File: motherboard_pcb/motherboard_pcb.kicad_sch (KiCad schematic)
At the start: 10 parts, among them J1 24 Power Supply Input, J2 Conn_01x04_Socket, J3 Conn_01x04_Socket, J4 Conn_01x04_Socket, J5 Conn_01x04_Socket, U1 ESP32-DEVKIT-V1

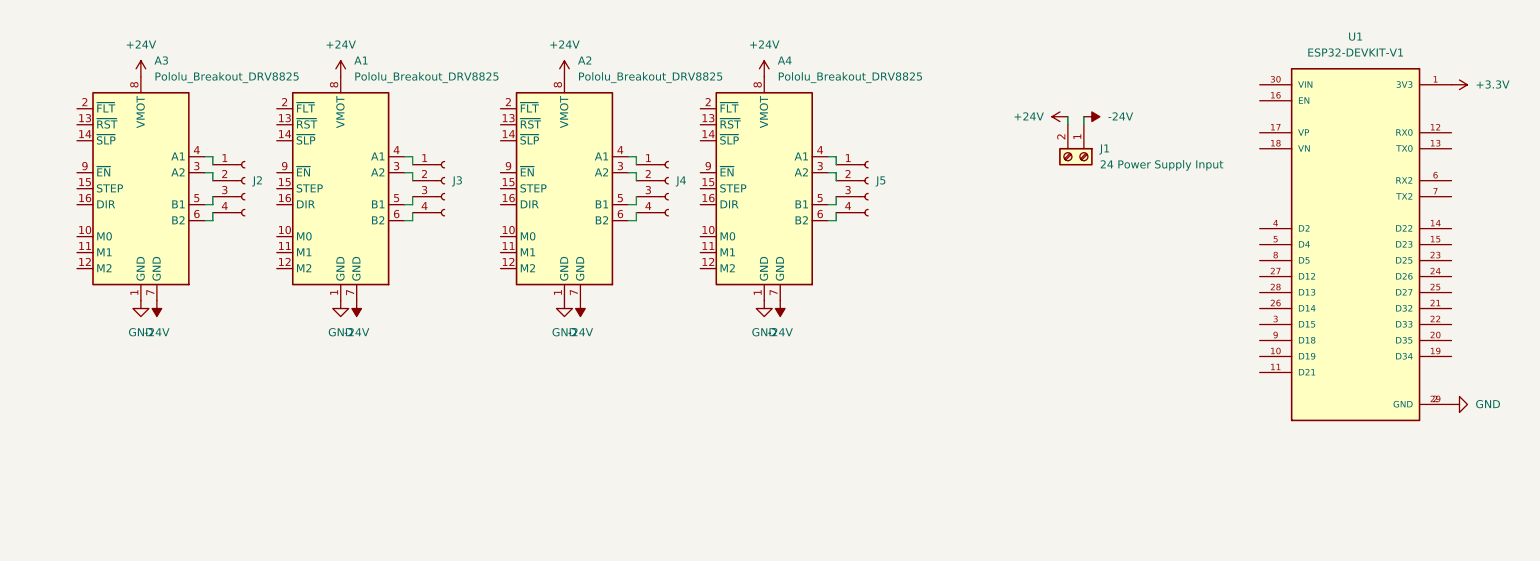
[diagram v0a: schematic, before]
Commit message: Added connections for OLED display
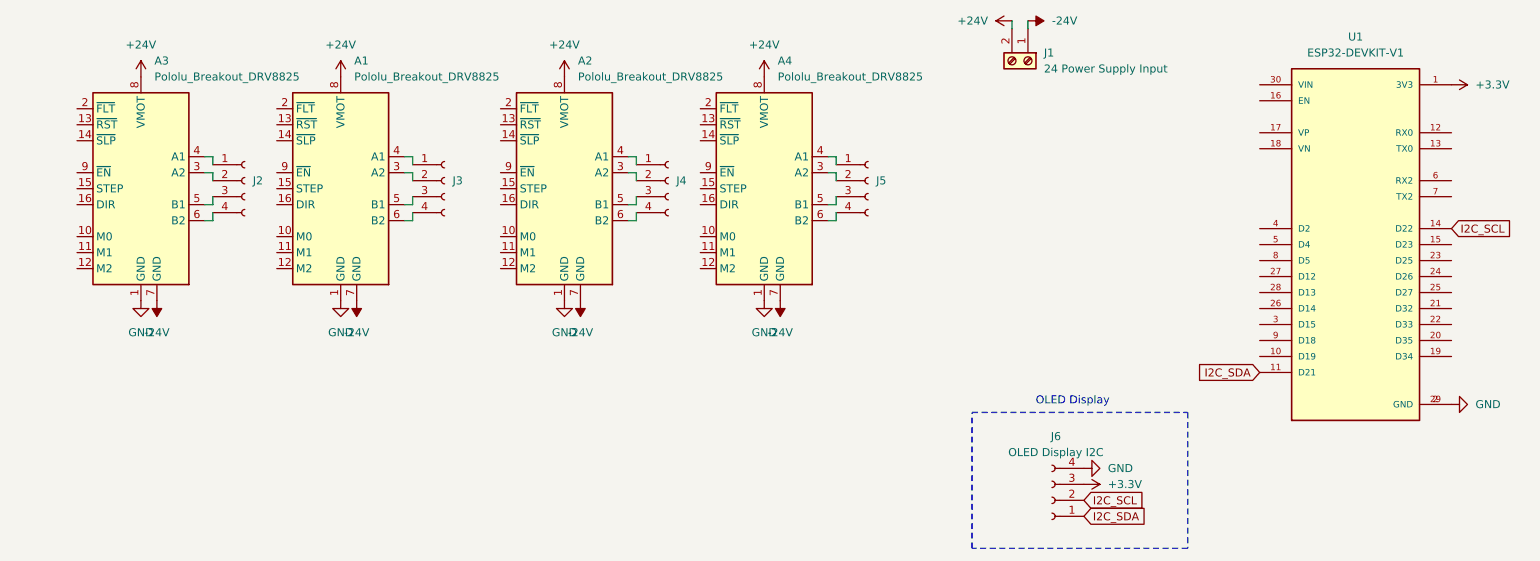
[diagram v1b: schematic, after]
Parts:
- added J6: OLED Display I2C, Connector_PinSocket_2.54mm:PinSocket_1x04_P2.54mm_Vertical, symbol Connector:Conn_01x04_Socket
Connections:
- net +3.3V: now also J6.3 (Pin_3)
- net GND: now also J6.4 (Pin_4)
- net I2C_SDA: now reaches U1.11 (D21)
- net I2C_SDA: now also J6.1 (Pin_1)
- net I2C_SCL: now reaches U1.14 (D22)
- net I2C_SCL: now also J6.2 (Pin_2)
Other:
- note added: "OLED Display"
- moved on the sheet: J1

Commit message: Added shift registers to the skematic and started attempting to route
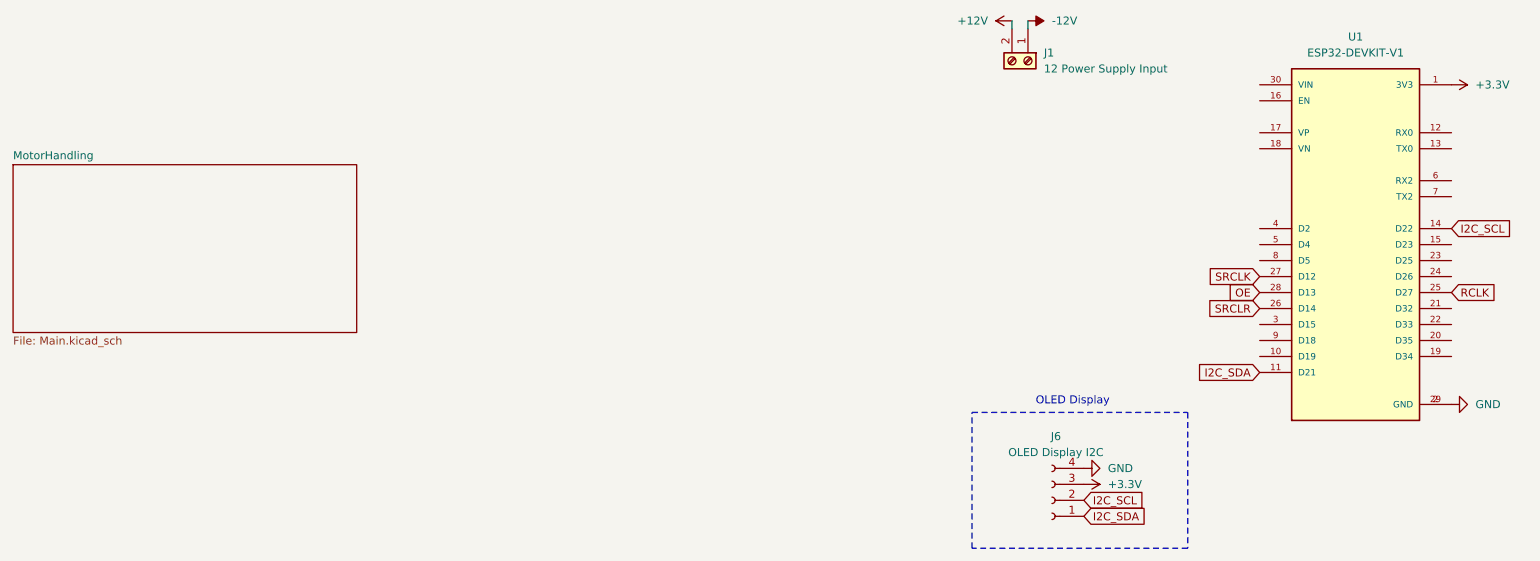
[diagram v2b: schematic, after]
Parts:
- removed A1, A2, A3, A4: Pololu_Breakout_DRV8825, Module:Pololu_Breakout-16_15.2x20.3mm, symbol Driver_Motor:Pololu_Breakout_DRV8825
- removed J2, J3, J4, J5: Conn_01x04_Socket, Connector_JST:JST_PH_B4B-PH-K_1x04_P2.00mm_Vertical, symbol Connector:Conn_01x04_Socket
- J1: value 24 Power Supply Input -> 12 Power Supply Input; footprint (none) -> TerminalBlock:TerminalBlock_Xinya_XY308-2.54-2P_1x02_P2.54mm_Horizontal
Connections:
- net RCLK: now reaches U1.25 (D27)
- net SRCLR: now reaches U1.26 (D14)
- net SRCLK: now reaches U1.27 (D12)
- net OE: now reaches U1.28 (D13)
- net +24V renamed +12V
- net -24V renamed -12V
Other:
- added sheet MotorHandling (Main.kicad_sch)

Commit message: Most of the motor stuff has been routed
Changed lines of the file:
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@@
 	)
 	(sheet
-		(at 20.32 39.37)
+		(at 140.97 45.72)
 		(size 54.61 26.67)
 		(exclude_from_sim no)
@@
 		)
 		(property "Sheetname" "MotorHandling"
-			(at 20.32 38.6584 0)
+			(at 140.97 45.0084 0)
 			(effects
 				(font
@@
 		)
 		(property "Sheetfile" "Main.kicad_sch"
-			(at 20.32 66.6246 0)
+			(at 140.97 72.9746 0)
 			(effects
 				(font

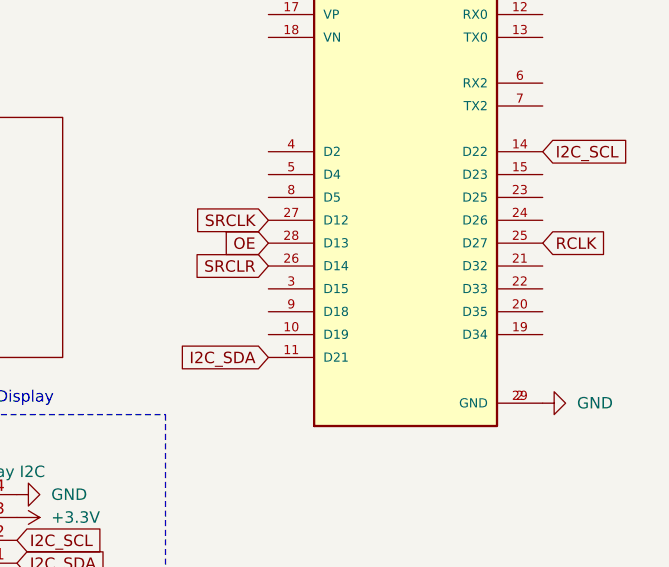
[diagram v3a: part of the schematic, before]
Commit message: Routed all connections to shift registers
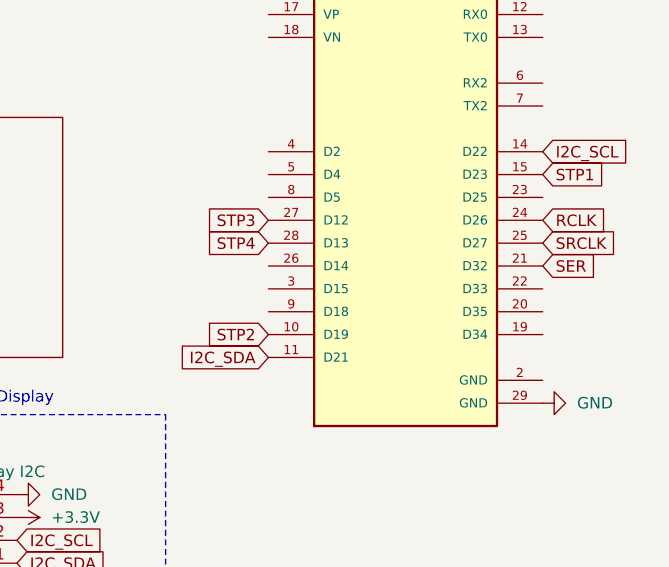
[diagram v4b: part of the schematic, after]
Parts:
- U1: footprint Library:MODULE_ESP32_DEVKIT_V1 -> ESP32-DEVKIT-V1:MODULE_ESP32_DEVKIT_V1
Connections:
- net GND: no longer U1.2 (GND)
- net RCLK: now also U1.24 (D26); no longer U1.25 (D27)
- net SRCLK: now also U1.25 (D27); no longer U1.27 (D12)
- net STP2: now reaches U1.10 (D19)
- net STP1: now reaches U1.15 (D23)
- net SER: now reaches U1.21 (D32)
- net OE renamed STP4
- net SRCLR: no longer names the net of U1.26 (D14)
- new net STP3: U1.27 (D12)
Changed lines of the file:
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@@
 		)
 	)
-	(global_label "OE"
+	(global_label "I2C_SDA"
+		(shape input)
+		(at 190.5 95.25 0)
+		(fields_autoplaced yes)
+		(effects
+			(font
+				(size 1.27 1.27)
+			)
+			(justify left)
+		)
+		(property "Intersheetrefs" "${INTERSHEET_REFS}"
+			(at 201.1052 95.25 0)
+			(effects
+				(font
+					(size 1.27 1.27)
+				)
+				(justify left)
+				(hide yes)
+			)
+		)
+	)
+	(global_label "STP1"
+		(shape input)
+		(at 248.92 52.07 0)
+		(fields_autoplaced yes)
+		(effects
+			(font
+				(size 1.27 1.27)
+			)
+			(justify left)
+		)
+		(property "Intersheetrefs" "${INTERSHEET_REFS}"
+			(at 256.5618 52.07 0)
+			(effects
+				(font
+					(size 1.27 1.27)
+				)
+				(justify left)
+				(hide yes)
+			)
+		)
+	)
+	(global_label "SER"
+		(shape input)
+		(at 248.92 62.23 0)
+		(fields_autoplaced yes)
+		(effects
+			(font
+				(size 1.27 1.27)
+			)
+			(justify left)
+		)
+		(property "Intersheetrefs" "${INTERSHEET_REFS}"
+			(at 255.5337 62.23 0)
+			(effects
+				(font
+					(size 1.27 1.27)
+				)
+				(justify left)
+				(hide yes)
+			)
+		)
+	)
+	(global_label "STP3"
+		(shape input)
+		(at 218.44 57.15 180)
+		(fields_autoplaced yes)
+		(effects
+			(font
+				(size 1.27 1.27)
+			)
+			(justify right)
+		)
+		(property "Intersheetrefs" "${INTERSHEET_REFS}"
+			(at 210.7982 57.15 0)
+			(effects
+				(font
+					(size 1.27 1.27)
+				)
+				(justify right)
+				(hide yes)
+			)
+		)
+	)
+	(global_label "STP4"
 		(shape input)
 		(at 218.44 59.69 180)
@@
 		)
 		(property "Intersheetrefs" "${INTERSHEET_REFS}"
-			(at 212.9753 59.69 0)
+			(at 210.7982 59.69 0)
 			(effects
 				(font
@@
 		)
 	)
-	(global_label "I2C_SDA"
-		(shape input)
-		(at 190.5 95.25 0)
-		(fields_autoplaced yes)
-		(effects
-			(font
-				(size 1.27 1.27)
-			)
-			(justify left)
-		)
-		(property "Intersheetrefs" "${INTERSHEET_REFS}"
-			(at 201.1052 95.25 0)
-			(effects
-				(font
-					(size 1.27 1.27)
-				)
-				(justify left)
-				(hide yes)
-			)
-		)
-	)
-	(global_label "SRCLR"
-		(shape input)
-		(at 218.44 62.23 180)
+	(global_label "RCLK"
+		(shape input)
+		(at 248.92 57.15 0)
+		(fields_autoplaced yes)
+		(effects
+			(font
+				(size 1.27 1.27)
+			)
+			(justify left)
+		)
+		(property "Intersheetrefs" "${INTERSHEET_REFS}"
+			(at 256.7433 57.15 0)
+			(effects
+				(font
+					(size 1.27 1.27)
+				)
+				(justify left)
+				(hide yes)
+			)
+		)
+	)
+	(global_label "I2C_SCL"
+		(shape input)
+		(at 248.92 49.53 0)
+		(fields_autoplaced yes)
+		(effects
+			(font
+				(size 1.27 1.27)
+			)
+			(justify left)
+		)
+		(property "Intersheetrefs" "${INTERSHEET_REFS}"
+			(at 259.4647 49.53 0)
+			(effects
+				(font
+					(size 1.27 1.27)
+				)
+				(justify left)
+				(hide yes)
+			)
+		)
+	)
+	(global_label "I2C_SCL"
+		(shape input)
+		(at 190.5 92.71 0)
+		(fields_autoplaced yes)
+		(effects
+			(font
+				(size 1.27 1.27)
+			)
+			(justify left)
+		)
+		(property "Intersheetrefs" "${INTERSHEET_REFS}"
+			(at 201.0447 92.71 0)
+			(effects
+				(font
+					(size 1.27 1.27)
+				)
+				(justify left)
+				(hide yes)
+			)
+		)
+	)
+	(global_label "STP2"
+		(shape input)
+		(at 218.44 69.85 180)
 		(fields_autoplaced yes)
 		(effects
@@
 		)
 		(property "Intersheetrefs" "${INTERSHEET_REFS}"
-			(at 209.4072 62.23 0)
+			(at 210.7982 69.85 0)
 			(effects
 				(font
@@
 		)
 	)
-	(global_label "RCLK"
+	(global_label "SRCLK"
 		(shape input)
 		(at 248.92 59.69 0)
@@
 		)
 		(property "Intersheetrefs" "${INTERSHEET_REFS}"
-			(at 256.7433 59.69 0)
-			(effects
-				(font
-					(size 1.27 1.27)
-				)
-				(justify left)
-				(hide yes)
-			)
-		)
-	)
-	(global_label "I2C_SCL"
-		(shape input)
-		(at 248.92 49.53 0)
-		(fields_autoplaced yes)
-		(effects
-			(font
-				(size 1.27 1.27)
-			)
-			(justify left)
-		)
-		(property "Intersheetrefs" "${INTERSHEET_REFS}"
-			(at 259.4647 49.53 0)
-			(effects
-				(font
-					(size 1.27 1.27)
-				)
-				(justify left)
-				(hide yes)
-			)
-		)
-	)
-	(global_label "I2C_SCL"
-		(shape input)
-		(at 190.5 92.71 0)
-		(fields_autoplaced yes)
-		(effects
-			(font
-				(size 1.27 1.27)
-			)
-			(justify left)
-		)
-		(property "Intersheetrefs" "${INTERSHEET_REFS}"
-			(at 201.0447 92.71 0)
-			(effects
-				(font
-					(size 1.27 1.27)
-				)
-				(justify left)
-				(hide yes)
-			)
-		)
-	)
-	(global_label "SRCLK"
-		(shape input)
-		(at 218.44 57.15 180)
-		(fields_autoplaced yes)
-		(effects
-			(font
-				(size 1.27 1.27)
-			)
-			(justify right)
-		)
-		(property "Intersheetrefs" "${INTERSHEET_REFS}"
-			(at 209.4072 57.15 0)
-			(effects
-				(font
-					(size 1.27 1.27)
-				)
-				(justify right)
+			(at 257.9528 59.69 0)
+			(effects
+				(font
+					(size 1.27 1.27)
+				)
+				(justify left)
 				(hide yes)
 			)
@@
 			)
 		)
-		(property "Footprint" "Library:MODULE_ESP32_DEVKIT_V1"
+		(property "Footprint" "ESP32-DEVKIT-V1:MODULE_ESP32_DEVKIT_V1"
 			(at 233.68 52.07 0)
 			(effects
